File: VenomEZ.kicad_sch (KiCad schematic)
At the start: 41 parts, among them CN1 HC-XH-5A-G, CN10 HC-XH-2A-G, CN2 HC-PH-8A-G, CN3 HC-XH-8A-G, CN4 HC-XH-8A-G, CN5 HC-XH-2A-G, CN6 HC-PH-7A-G, CN7 HC-XH-2A-G, CN8 HC-XH-2A-G, CN9 HC-XH-2A-G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

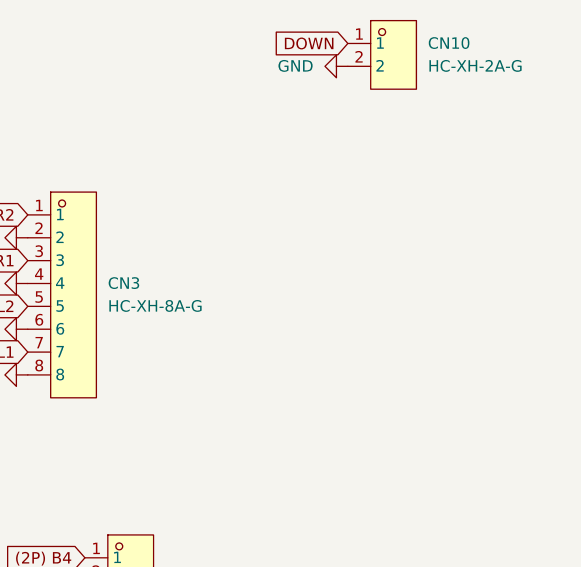
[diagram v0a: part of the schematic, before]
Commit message: Started og usb connector / redesign
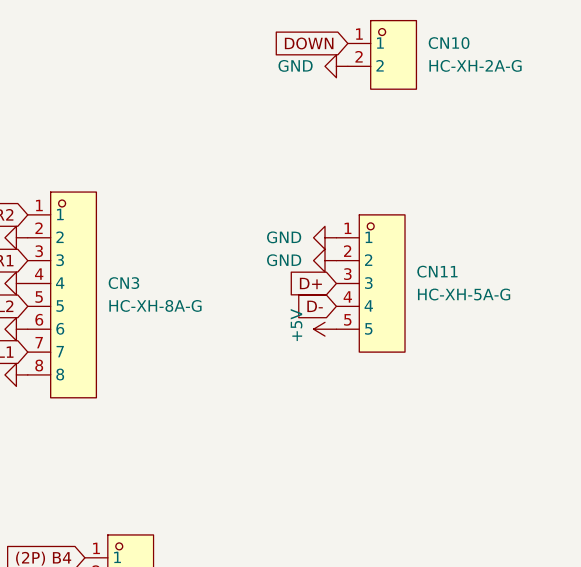
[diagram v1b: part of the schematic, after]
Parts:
- added CN11: HC-XH-5A-G, easyeda2kicad:CONN-TH_5P-P2.50_HC-XH-5A-G, symbol easyeda2kicad:HC-XH-5A-G
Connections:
- net +5V: now also CN11.5
- net D+: now also CN11.3
- net D-: now also CN11.4
- net GND: now also CN11.1, CN11.2
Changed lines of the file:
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@@
+    )
+  )
+  (global_label "D+" (shape input) (at 255.27 81.28 180)
+    (effects (font (size 1.27 1.27)) (justify right))
+    (property "Intersheetrefs" "${INTERSHEET_REFS}" (at 255.27 81.28 0)
+      (effects (font (size 1.27 1.27)) hide)
     )
   )
@@
     (property "Intersheetrefs" "${INTERSHEET_REFS}" (at 109.3439 118.11 0)
       (effects (font (size 1.27 1.27)) (justify left) hide)
+    )
+  )
+  (global_label "D-" (shape input) (at 255.27 83.82 180)
+    (effects (font (size 1.27 1.27)) (justify right))
+    (property "Intersheetrefs" "${INTERSHEET_REFS}" (at 255.27 83.82 0)
+      (effects (font (size 1.27 1.27)) hide)
     )
   )
@@
     )
   )
+  (symbol (lib_id "power:+5V") (at 255.27 86.36 90) (unit 1)
+    (in_bom yes) (on_board yes) (dnp no)
+    (property "Reference" "#PWR041" (at 259.08 86.36 0)
+      (effects (font (size 1.27 1.27)) hide)
+    )
+    (property "Value" "+5V" (at 250.8758 85.979 0)
+      (effects (font (size 1.27 1.27)))
+    )
+    (property "Footprint" "" (at 255.27 86.36 0)
+      (effects (font (size 1.27 1.27)) hide)
+    )
+    (property "Datasheet" "" (at 255.27 86.36 0)
+      (effects (font (size 1.27 1.27)) hide)
+    )
+    (pin "1")
+    (instances
+      (project "VenomEZ"
+        (path "/9bda465f-e399-4153-b93d-135c505ebd4f"
+          (reference "#PWR041") (unit 1)
+        )
+      )
+      (project "Flatbox-rev4"
+        (path "/fd23c70e-ae4a-4895-b78d-a20f7a3107ca"
+          (reference "#PWR022") (unit 1)
+        )
+      )
+    )
+  )
   (symbol (lib_id "Device:C_Small") (at 110.49 22.86 0) (unit 1)
     (in_bom yes) (on_board yes) (dnp no)
@@
     )
   )
+  (symbol (lib_id "easyeda2kicad:HC-XH-5A-G") (at 260.35 81.28 0) (unit 1)
+    (in_bom yes) (on_board yes) (dnp no) (fields_autoplaced)
+    (property "Reference" "CN11" (at 264.16 80.01 0)
+      (effects (font (size 1.27 1.27)) (justify left))
+    )
+    (property "Value" "HC-XH-5A-G" (at 264.16 82.55 0)
+      (effects (font (size 1.27 1.27)) (justify left))
+    )
+    (property "Footprint" "easyeda2kicad:CONN-TH_5P-P2.50_HC-XH-5A-G" (at 260.35 93.98 0)
+      (effects (font (size 1.27 1.27)) hide)
+    )
+    (property "Datasheet" "" (at 260.35 81.28 0)
+      (effects (font (size 1.27 1.27)) hide)
+    )
+    (property "Manufacturer" "HCTL(华灿天禄)" (at 260.35 96.52 0)
+      (effects (font (size 1.27 1.27)) hide)
+    )
+    (property "LCSC Part" "C5341204" (at 260.35 99.06 0)
+      (effects (font (size 1.27 1.27)) hide)
+    )
+    (property "JLC Part" "Extended Part" (at 260.35 101.6 0)
+      (effects (font (size 1.27 1.27)) hide)
+    )
+    (pin "1")
+    (pin "2")
+    (pin "3")
+    (pin "4")
+    (pin "5")
+    (instances
+      (project "VenomEZ"
+        (path "/9bda465f-e399-4153-b93d-135c505ebd4f"
+          (reference "CN11") (unit 1)
+        )
+      )
+    )
+  )
   (symbol (lib_id "power:GND") (at 92.71 38.1 0) (unit 1)
     (in_bom yes) (on_board yes) (dnp no)
@@
         (path "/9bda465f-e399-4153-b93d-135c505ebd4f"
           (reference "#PWR036") (unit 1)
+        )
+      )
+    )
+  )
+  (symbol (lib_id "power:GND") (at 255.27 76.2 270) (unit 1)
+    (in_bom yes) (on_board yes) (dnp no) (fields_autoplaced)
+    (property "Reference" "#PWR039" (at 248.92 76.2 0)
+      (effects (font (size 1.27 1.27)) hide)
+    )
+    (property "Value" "GND" (at 251.46 76.2 90)
+      (effects (font (size 1.27 1.27)) (justify right))
+    )
+    (property "Footprint" "" (at 255.27 76.2 0)
+      (effects (font (size 1.27 1.27)) hide)
+    )
+    (property "Datasheet" "" (at 255.27 76.2 0)
+      (effects (font (size 1.27 1.27)) hide)
+    )
+    (pin "1")
+    (instances
+      (project "VenomEZ"
+        (path "/9bda465f-e399-4153-b93d-135c505ebd4f"
+          (reference "#PWR039") (unit 1)
         )
       )
@@
         )
       )
+    )
+  )
+  (symbol (lib_id "power:GND") (at 255.27 78.74 270) (unit 1)
+    (in_bom yes) (on_board yes) (dnp no) (fields_autoplaced)
+    (property "Reference" "#PWR040" (at 248.92 78.74 0)
+      (effects (font (size 1.27 1.27)) hide)
+    )
+    (property "Value" "GND" (at 251.46 78.74 90)
+      (effects (font (size 1.27 1.27)) (justify right))
+    )
+    (property "Footprint" "" (at 255.27 78.74 0)
+      (effects (font (size 1.27 1.27)) hide)
+    )
+    (property "Datasheet" "" (at 255.27 78.74 0)
+      (effects (font (size 1.27 1.27)) hide)
+    )
+    (pin "1")
+    (instances
+      (project "VenomEZ"
+        (path "/9bda465f-e399-4153-b93d-135c505ebd4f"
+          (reference "#PWR040") (unit 1)
+        )
+      )

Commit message: Move lcsc symbols to their own library
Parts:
- CN1, CN11: footprint easyeda2kicad:CONN-TH_5P-P2.50_HC-XH-5A-G -> lcsc:CONN-TH_5P-P2.50_HC-XH-5A-G
- CN10, CN5, CN7, CN8, CN9: footprint easyeda2kicad:CONN-TH_2P-P2.50_HC-XH-2A-G -> lcsc:CONN-TH_2P-P2.50_HC-XH-2A-G
- CN2: footprint easyeda2kicad:CONN-TH_8P-P2.00_PH-8A -> lcsc:CONN-TH_8P-P2.00_PH-8A
- CN3, CN4: footprint easyeda2kicad:CONN-TH_8P-P2.50_HCTL_XH-8A_C2908606 -> lcsc:CONN-TH_8P-P2.50_HCTL_XH-8A_C2908606
- CN6: footprint easyeda2kicad:CONN-TH_7P-P2.00_PH-7A -> lcsc:CONN-TH_7P-P2.00_PH-7A
- SW1, SW2, SW3: footprint easyeda2kicad:SW-SMD_4P-L3.6-W3.0-P1.50-LS4.7 -> lcsc:SW-SMD_4P-L3.6-W3.0-P1.50-LS4.7
- U2: footprint easyeda2kicad:SOIC-8_L5.3-W5.3-P1.27-LS8.0-BL -> lcsc:SOIC-8_L5.3-W5.3-P1.27-LS8.0-BL
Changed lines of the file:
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@@
       (effects (font (size 1.27 1.27)) (justify left))
     )
-    (property "Footprint" "easyeda2kicad:CONN-TH_2P-P2.50_HC-XH-2A-G" (at 261.62 54.61 0)
+    (property "Footprint" "lcsc:CONN-TH_2P-P2.50_HC-XH-2A-G" (at 261.62 54.61 0)
       (effects (font (size 1.27 1.27)) hide)
     )
@@
       (effects (font (size 1.27 1.27)) (justify left))
     )
-    (property "Footprint" "easyeda2kicad:CONN-TH_5P-P2.50_HC-XH-5A-G" (at 193.04 91.44 0)
+    (property "Footprint" "lcsc:CONN-TH_5P-P2.50_HC-XH-5A-G" (at 193.04 91.44 0)
       (effects (font (size 1.27 1.27)) hide)
     )
@@
       (effects (font (size 1.27 1.27)))
     )
-    (property "Footprint" "easyeda2kicad:SW-SMD_4P-L3.6-W3.0-P1.50-LS4.7" (at 195.58 71.12 0)
+    (property "Footprint" "lcsc:SW-SMD_4P-L3.6-W3.0-P1.50-LS4.7" (at 195.58 71.12 0)
       (effects (font (size 1.27 1.27)) hide)
     )
@@
       (effects (font (size 1.27 1.27)) (justify left))
     )
-    (property "Footprint" "easyeda2kicad:CONN-TH_2P-P2.50_HC-XH-2A-G" (at 261.62 34.29 0)
+    (property "Footprint" "lcsc:CONN-TH_2P-P2.50_HC-XH-2A-G" (at 261.62 34.29 0)
       (effects (font (size 1.27 1.27)) hide)
     )
@@
       (effects (font (size 1.27 1.27)) (justify left))
     )
-    (property "Footprint" "easyeda2kicad:CONN-TH_8P-P2.50_HCTL_XH-8A_C2908606" (at 226.06 99.06 0)
+    (property "Footprint" "lcsc:CONN-TH_8P-P2.50_HCTL_XH-8A_C2908606" (at 226.06 99.06 0)
       (effects (font (size 1.27 1.27)) hide)
     )
@@
       (effects (font (size 1.27 1.27)))
     )
-    (property "Footprint" "easyeda2kicad:SOIC-8_L5.3-W5.3-P1.27-LS8.0-BL" (at 114.3 243.84 0)
+    (property "Footprint" "lcsc:SOIC-8_L5.3-W5.3-P1.27-LS8.0-BL" (at 114.3 243.84 0)
       (effects (font (size 1.27 1.27)) hide)
     )
@@
       (effects (font (size 1.27 1.27)))
     )
-    (property "Footprint" "easyeda2kicad:SW-SMD_4P-L3.6-W3.0-P1.50-LS4.7" (at 195.58 40.64 0)
+    (property "Footprint" "lcsc:SW-SMD_4P-L3.6-W3.0-P1.50-LS4.7" (at 195.58 40.64 0)
       (effects (font (size 1.27 1.27)) hide)
     )
@@
       (effects (font (size 1.27 1.27)) (justify left))
     )
-    (property "Footprint" "easyeda2kicad:CONN-TH_5P-P2.50_HC-XH-5A-G" (at 260.35 93.98 0)
+    (property "Footprint" "lcsc:CONN-TH_5P-P2.50_HC-XH-5A-G" (at 260.35 93.98 0)
       (effects (font (size 1.27 1.27)) hide)
     )
@@
       (effects (font (size 1.27 1.27)) (justify left))
     )
-    (property "Footprint" "easyeda2kicad:CONN-TH_8P-P2.50_HCTL_XH-8A_C2908606" (at 232.41 137.16 0)
+    (property "Footprint" "lcsc:CONN-TH_8P-P2.50_HCTL_XH-8A_C2908606" (at 232.41 137.16 0)
       (effects (font (size 1.27 1.27)) hide)
     )
@@
       (effects (font (size 1.27 1.27)) (justify left))
     )
-    (property "Footprint" "easyeda2kicad:CONN-TH_8P-P2.00_PH-8A" (at 193.04 137.16 0)
+    (property "Footprint" "lcsc:CONN-TH_8P-P2.00_PH-8A" (at 193.04 137.16 0)
       (effects (font (size 1.27 1.27)) hide)
     )
@@
       (effects (font (size 1.27 1.27)) (justify left))
     )
-    (property "Footprint" "easyeda2kicad:CONN-TH_2P-P2.50_HC-XH-2A-G" (at 261.62 44.45 0)
+    (property "Footprint" "lcsc:CONN-TH_2P-P2.50_HC-XH-2A-G" (at 261.62 44.45 0)
       (effects (font (size 1.27 1.27)) hide)
     )
@@
       (effects (font (size 1.27 1.27)))
     )
-    (property "Footprint" "easyeda2kicad:SW-SMD_4P-L3.6-W3.0-P1.50-LS4.7" (at 195.58 55.88 0)
+    (property "Footprint" "lcsc:SW-SMD_4P-L3.6-W3.0-P1.50-LS4.7" (at 195.58 55.88 0)
       (effects (font (size 1.27 1.27)) hide)
     )
@@
       (effects (font (size 1.27 1.27)) (justify left))
     )
-    (property "Footprint" "easyeda2kicad:CONN-TH_2P-P2.50_HC-XH-2A-G" (at 191.77 105.41 0)
+    (property "Footprint" "lcsc:CONN-TH_2P-P2.50_HC-XH-2A-G" (at 191.77 105.41 0)
       (effects (font (size 1.27 1.27)) hide)
     )
@@
       (effects (font (size 1.27 1.27)) (justify left))
     )
-    (property "Footprint" "easyeda2kicad:CONN-TH_2P-P2.50_HC-XH-2A-G" (at 261.62 64.77 0)
+    (property "Footprint" "lcsc:CONN-TH_2P-P2.50_HC-XH-2A-G" (at 261.62 64.77 0)
       (effects (font (size 1.27 1.27)) hide)
     )
@@
       (effects (font (size 1.27 1.27)) (justify left))
     )
-    (property "Footprint" "easyeda2kicad:CONN-TH_7P-P2.00_PH-7A" (at 193.04 167.64 0)
-      (effects (font (size 1.27 1.27)) hide)
-    )
+    (property "Footprint" "lcsc:CONN-TH_7P-P2.00_PH-7A" (at 193.04 167.64 0)
+      (effects (font (size 1.27 1.27)) hide)
+    )
